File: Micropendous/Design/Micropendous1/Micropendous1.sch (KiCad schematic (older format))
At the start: 52 parts, among them IC1 AT90USB16, J1 USBCONN, K1 Vcc_Sel, P1 Micropendous1, SW1 RESET, SW2 HWB, U1 VIA, U14 VIA, U2 VIA, U25 VIA, U27 VIA, U28 VIA, U29 VIA, U3 VIA, U30 VIA, U31 VIA, U32 VIA, U33 VIA, U34 VIA, U35 VIA, U36 VIA, U37 VIA, U38 VIA, U39 VIA, U4 VIA, U40 VIA, U41 VIA, U42 VIA, U43 VIA, U5 VIA, X1 8MHz

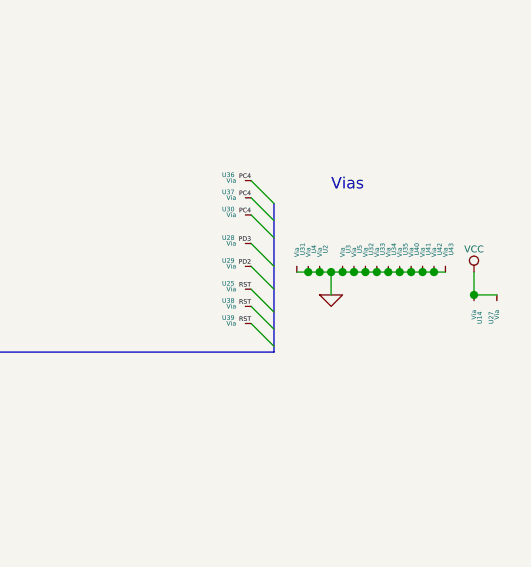
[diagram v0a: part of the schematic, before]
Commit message: Updated Micropendous1 design to 8mil-8mil-20mil.
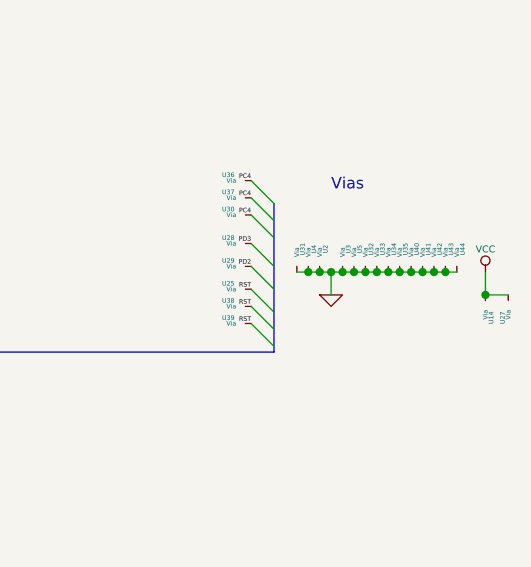
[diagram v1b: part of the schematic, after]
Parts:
- added U44: VIA, symbol VIA
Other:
- moved on the sheet: U14, U27
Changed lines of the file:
@@
-EESchema Schematic File Version 2  date 4/23/2009 5:51:20 PM
-LIBS:opendous,power,device,conn,linear,regul,74xx,cmos4000,adc-dac,memory,xilinx,special,microcontrollers,dsp,microchip,analog_switches,motorola,texas,intel,audio,interface,digital-audio,philips,display,cypress,siliconi,opto,atmel,contrib,valves,transistors,.\Micropendous1.cache
+EESchema Schematic File Version 2  date 29/08/2010 20:58:34
+LIBS:power
+LIBS:device
+LIBS:transistors
+LIBS:conn
+LIBS:linear
+LIBS:regul
+LIBS:74xx
+LIBS:cmos4000
+LIBS:adc-dac
+LIBS:memory
+LIBS:xilinx
+LIBS:special
+LIBS:microcontrollers
+LIBS:dsp
+LIBS:microchip
+LIBS:analog_switches
+LIBS:motorola
+LIBS:texas
+LIBS:intel
+LIBS:audio
+LIBS:interface
+LIBS:digital-audio
+LIBS:philips
+LIBS:display
+LIBS:cypress
+LIBS:siliconi
+LIBS:opto
+LIBS:atmel
+LIBS:contrib
+LIBS:valves
+LIBS:opendous
+LIBS:Micropendous1-cache
 EELAYER 24  0
 EELAYER END
@@
 Sheet 1 1
 Title "Micropendous1"
-Date "23 apr 2009"
+Date "30 aug 2010"
 Rev "1.0"
 Comp ""
@@
 $EndDescr
 Connection ~ 10250 4850
-Wire Wire Line
-	10300 4850 9650 4850
 Connection ~ 10100 4850
 Connection ~ 10050 4850
@@
 	7250 5000 7250 4900
 Wire Wire Line
-	10425 4850 10425 4950
+	10475 4850 10475 4950
 Wire Wire Line
 	7100 3775 7100 4025
@@
 Connection ~ 9950 4850
 Wire Wire Line
-	10425 4950 10525 4950
-Connection ~ 10425 4950
+	10475 4950 10575 4950
+Connection ~ 10475 4950
 Wire Wire Line
 	4250 6100 4250 6200
@@
 Connection ~ 10150 4850
 Connection ~ 10200 4850
+Wire Wire Line
+	10350 4850 9650 4850
+Connection ~ 10300 4850
+$Comp
+L VIA U44
+U 1 1 4C7B015B
+P 10350 4850
+F 0 "U44" V 10375 4950 20  0000 C CNN
+F 1 "VIA" H 10350 5050 60  0001 C CNN
+	1    10350 4850
+	1    0    0    -1
+$EndComp
 $Comp
 L VIA U43
@@
 L VCC #PWR02
 U 1 1 4949FDA8
-P 10425 4850
-F 0 "#PWR02" H 10425 4950 30  0001 C CNN
-F 1 "VCC" H 10425 4950 30  0000 C CNN
-	1    10425 4850
+P 10475 4850
+F 0 "#PWR02" H 10475 4950 30  0001 C CNN
+F 1 "VCC" H 10475 4950 30  0000 C CNN
+	1    10475 4850
 	1    0    0    -1
 $EndComp
@@
 L VIA U27
 U 1 1 4949FD98
-P 10525 4950
-F 0 "U27" V 10550 5050 20  0000 C CNN
-F 1 "VIA" H 10525 5150 60  0001 C CNN
-	1    10525 4950
+P 10575 4950
+F 0 "U27" V 10600 5050 20  0000 C CNN
+F 1 "VIA" H 10575 5150 60  0001 C CNN
+	1    10575 4950
 	-1   0    0    1
 $EndComp
@@
 L VIA U14
 U 1 1 4947E385
-P 10425 4950
-F 0 "U14" V 10450 5050 20  0000 C CNN
-F 1 "VIA" H 10425 5150 60  0001 C CNN
-	1    10425 4950
+P 10475 4950
+F 0 "U14" V 10500 5050 20  0000 C CNN
+F 1 "VIA" H 10475 5150 60  0001 C CNN
+	1    10475 4950
 	1    0    0    1
 $EndComp
